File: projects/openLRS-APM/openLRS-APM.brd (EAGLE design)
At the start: 43.1 x 20.7 mm, 29 parts, among them IC1 MCP1703CB, IC2 RFM23BPSMD, J1 AVR_SPI_PRG_6PTH, U1 ATMEGA328P, Y1 16MHz

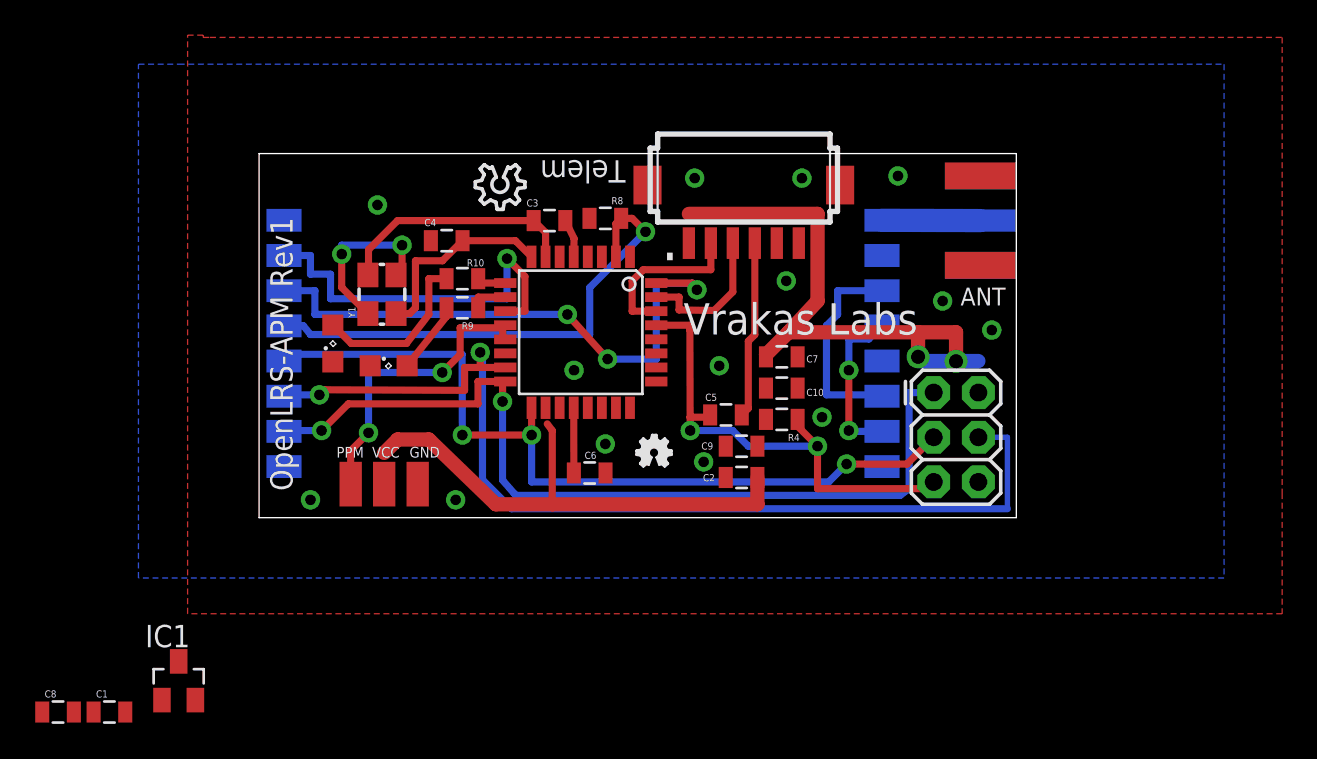
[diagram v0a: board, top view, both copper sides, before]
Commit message: Initial Rev2 Commit
Rearranged for shrink wrapping, fixed voltage levels. may need routing
touch up.
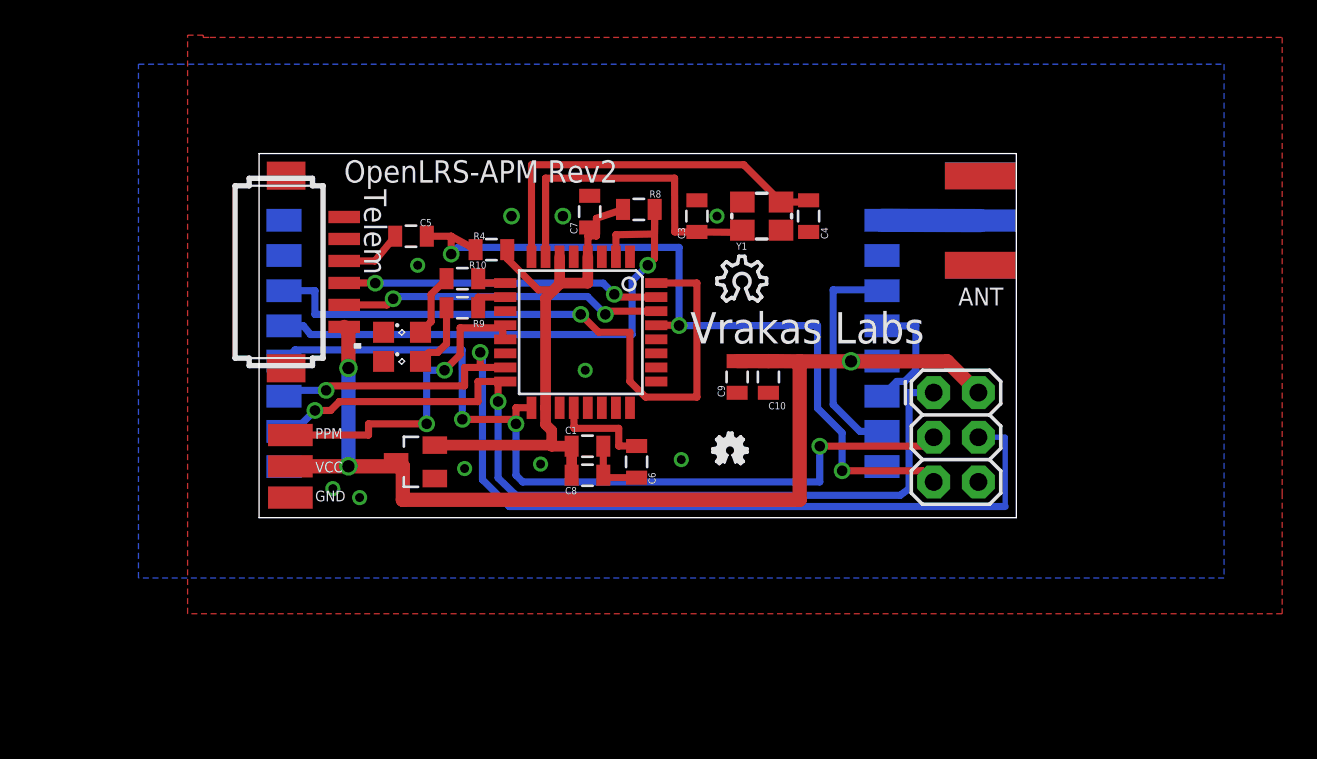
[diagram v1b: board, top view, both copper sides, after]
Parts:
- removed C2: 100n, SparkFun-Capacitors:0805
- moved U$3 40.9 mm to (42.7, 8.89), turned to 0 degrees
- moved C8 33.0 mm to (18.7, 2.41)
- moved C1 31.1 mm to (18.7, 4.06)
- moved TELEMETRY 23.8 mm to (3.94, 14.0), turned to 90 degrees
- moved Y1 22.0 mm to (28.6, 17.1), turned to 180 degrees
- moved C4 20.6 mm to (31.2, 17.1), turned to 270 degrees
- moved C5 20.6 mm to (8.64, 16.0), turned to 0 degrees
- moved R4 19.1 mm to (13.2, 15.2), turned to 0 degrees
- moved IC1 18.3 mm to (8.89, 3.17), turned to 90 degrees
- moved C7 13.7 mm to (18.8, 17.4), turned to 90 degrees
- moved U$2 13.4 mm to (26.0, 12.3), turned to 0 degrees
- moved C3 8.39 mm to (24.9, 17.1), turned to 90 degrees
- moved GND 7.28 mm to (1.78, 1.14), turned to 270 degrees
- moved VCC 5.43 mm to (1.78, 2.92), turned to 270 degrees
- moved PPM 4.42 mm to (1.78, 4.70), turned to 90 degrees
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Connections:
- removed net SDN: IC2.15, U1.11
- removed net VCC: C2.1, C7.1, R8.2
- net 3V: now also C7.1, R8.2
- net GND: now also IC2.15; no longer C2.2
- net N$1: now also IC2.7; no longer IC2.6
- net N$2: now also IC2.6; no longer IC2.7
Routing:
- net 5V: track 0.00 -> 63.4 mm, vias 0 -> 3
- net VCC: track 62.6 -> 0.00 mm, vias 2 -> 0
- net 3V: track 0.00 -> 32.5 mm
- net SDN: track 22.1 -> 0.00 mm, vias 1 -> 0
- net /RESET: track 27.9 -> 45.5 mm, vias 2 -> 3
- net N$12: track 11.4 -> 22.0 mm
- net TXD: track 8.29 -> 18.1 mm, vias 0 -> 2
- net RXD: track 9.34 -> 18.4 mm, vias 0 -> 2
- net GND: track 12.2 -> 3.70 mm, vias 16 -> 10
- net DTR: track 10.1 -> 3.57 mm
- net N$9: track 9.75 -> 3.66 mm
- net N$11: track 13.9 -> 18.8 mm
- net RF_IRQ: track 33.4 -> 37.2 mm, vias 3 -> 1
- net RF_CS: track 28.8 -> 32.5 mm
- net N$2: track 9.29 -> 7.00 mm, vias 2 -> 0
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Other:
- board text added: "OpenLRS-APM Rev2"
- board text removed: "OpenLRS-APM Rev1"

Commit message: Initial 32u4 USB dongle version
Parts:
- removed C7: 100n, SparkFun-Capacitors:0805
- removed GND, PPM, VCC: (no value), wirepad:SMD1,27-2,54
- removed R8: 1k, SparkFun-Resistors:0805
- removed TELEMETRY: DF13-6P-1.25H, con-hirose-df13:DF13A-6P-1.25H
- removed U1: ATMEGA328P, SparkFun-DigitalIC:TQFP32-08
- added C11: 100n, SparkFun-Capacitors:0805
- added C2: 1uF, SparkFun-Capacitors:0805
- added JP1: USB-A-H, SparkFun-Connectors:USB-A-H
- added MCU1: ATMEGA32U4TQFP, SparkFun-DigitalIC:SPARKFUN-DIGITALIC_TQFP44
- added R1, R2: 22, SparkFun-Resistors:0805
- C5: value 100n -> 1uF
- J1: value AVR_SPI_PRG_6PTH -> CON_HEADER_PRG_AVR_ICSP-SMD; device SparkFun-Connectors:2X3 -> dp_devices:M2X3_SMD
- moved U$3 31.7 mm to (11.0, 8.39), flipped to the top
- moved LED2 27.3 mm to (34.4, 17.8), turned to 270 degrees
- moved LED1 25.7 mm to (32.2, 17.8), turned to 270 degrees
- moved R10 22.8 mm to (34.4, 14.0), turned to 270 degrees
- moved R9 20.7 mm to (32.2, 14.0), turned to 270 degrees
- moved U$2 20.0 mm to (6.43, 16.1)
- moved C4 18.9 mm to (20.9, 1.27), turned to 180 degrees
- moved U$1 17.5 mm to (37.6, 15.9)
- moved C6 16.6 mm to (15.4, 18.6), turned to 0 degrees
- moved Y1 15.5 mm to (25.4, 2.00), turned to 0 degrees
- moved C3 15.0 mm to (29.3, 2.80), turned to 0 degrees
- moved C9 13.0 mm to (39.3, 12.6), turned to 90 degrees
- moved R4 12.7 mm to (20.2, 4.60)
- moved C10 9.01 mm to (36.7, 12.6), turned to 90 degrees
- moved SMA 7.28 mm to (50.1, 14.9)
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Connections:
- removed net DTR: C5.1, TELEMETRY.P$4
- removed net N$14: C6.2, U1.20
- removed net PPM: PPM.1, U1.12, U1.13
- removed net RF_CS: IC2.13, R8.1, U1.2
- removed net RF_IRQ: IC2.14, U1.32
- removed net RXD: TELEMETRY.P$2, U1.30
- removed net TXD: TELEMETRY.P$3, U1.31
- new net CS: IC2.13, MCU1.30
- new net D_N: MCU1.3, R2.1
- new net D_P: MCU1.4, R1.1
- new net IRQ: IC2.14, MCU1.18
- new net N$3: C6.2, MCU1.42
- new net R_N: JP1.D-, R2.2
- new net R_P: JP1.D+, R1.2
- new net UCAP: C5.1, MCU1.6
- net /RESET: now also MCU1.13; no longer C5.2, U1.29
- net 3V: now also MCU1.14, MCU1.24, MCU1.34, MCU1.44; no longer C7.1, R8.2, U1.18, U1.4, U1.6
- net 5V: now also C11.1, C2.1, JP1.VBUS, MCU1.2, MCU1.7; no longer TELEMETRY.P$1, VCC.1
- net GND: now also C11.2, C2.2, C5.2, JP1.GND, MCU1.15, MCU1.23, MCU1.35, MCU1.43, MCU1.5; no longer C7.2, GND.1, TELEMETRY.P$5, TELEMETRY.P$6, U1.21, U1.3, U1.5
- net MISO: now also MCU1.11; no longer U1.16
- net MOSI: now also MCU1.10; no longer U1.15
- net N$11: now also MCU1.17; no longer U1.7
- net N$12: now also MCU1.16; no longer U1.8
- net N$7: now also MCU1.28; no longer U1.10
- net N$8: now also MCU1.27; no longer U1.9
- net SCK: now also MCU1.9; no longer U1.17
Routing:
- net RF_IRQ: track 37.2 -> 0.00 mm, vias 1 -> 0
- net RF_CS: track 32.5 -> 0.00 mm, vias 1 -> 0
- net IRQ: track 0.00 -> 28.5 mm, vias 0 -> 3
- net CS: track 0.00 -> 24.9 mm, vias 0 -> 1
- net GND: track 3.70 -> 26.4 mm, vias 10 -> 30
- net PPM: track 18.6 -> 0.00 mm, vias 2 -> 0
- net RXD: track 18.4 -> 0.00 mm, vias 2 -> 0
- net TXD: track 18.1 -> 0.00 mm, vias 2 -> 0
- net 3V: track 32.5 -> 48.4 mm, vias 0 -> 4
- net MOSI: track 58.3 -> 43.9 mm, vias 2 -> 3
- net N$12: track 22.0 -> 11.1 mm
- net R_P: track 0.00 -> 9.59 mm
- net R_N: track 0.00 -> 9.58 mm
- net N$11: track 18.8 -> 9.49 mm
- net N$3: track 0.00 -> 8.80 mm, vias 0 -> 2
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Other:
- board size 43.1 x 20.7 mm -> 50 x 20 mm
- board text added: "ICSP"
- board text added: "Radio Modem"
- board text added: "USB"
- board text removed: "1"
- board text removed: "OpenLRS-APM Rev2"
- board text removed: "Telem"
